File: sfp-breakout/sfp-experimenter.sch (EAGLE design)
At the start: 49 parts, among them IC1 SN65LVDS1DBV, IC2 SN65LVDT2DBV, J1 694108106102, T1 BC847, T2 BC847, U1 LDO-MCP1825S, X1 PINHD-1X5LOCK, X2 PINHD-1X5LOCK, X3 PINHD-1X4LOCK

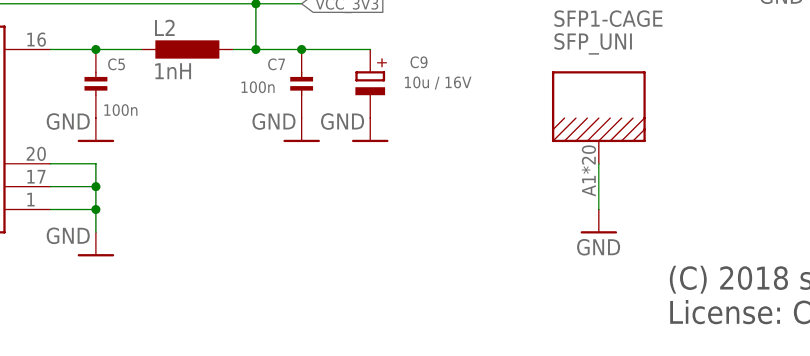
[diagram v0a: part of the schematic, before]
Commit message: sfp: add part numbers for SFP conn and cage
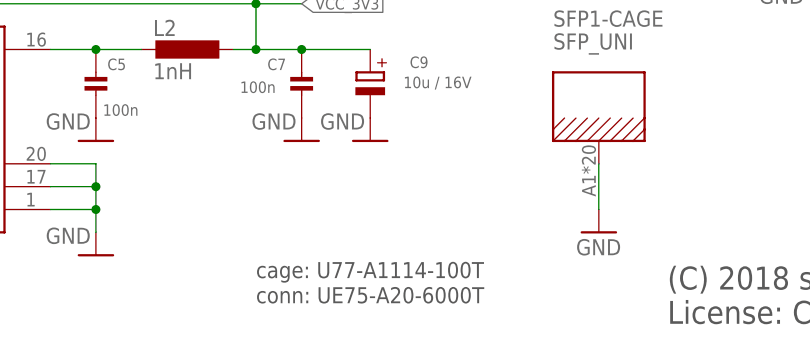
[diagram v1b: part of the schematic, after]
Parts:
- L1, L2: LINK UNKNOWN LINK -> https://www.digikey.de/product-detail/en/samsung-electro-me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
- SFP1: LINK UNKNOWN LINK -> https://www.digikey.de/products/en?keywords=U77-A1114-100TC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
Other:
- note added: "cage: U77-A1114-100T"
- note added: "conn: UE75-A20-6000T"
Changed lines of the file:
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@@
 <attribute name="CLASS" value="UNKNOWN CLASS"/>
 <attribute name="DESCRIPTION" value="NO DESCRIPTION"/>
-<attribute name="LINK" value="UNKNOWN LINK"/>
+<attribute name="LINK" value="https://www.digikey.de/products/en?keywords=U77-A1114-100TCT-ND"/>
 <attribute name="MANUFACTURER" value="UNKNOWN MANUFACTURER"/>
 <attribute name="MANUFACTURERPARTNUMBER" value="UNKNOWN MANUFACTURER PART NUMBER"/>
@@
 <attribute name="CLASS" value="INDUCTOR"/>
 <attribute name="DESCRIPTION" value="NO DESCRIPTION"/>
-<attribute name="LINK" value="UNKNOWN LINK"/>
+<attribute name="LINK" value="https://www.digikey.de/product-detail/en/samsung-electro-mechanics/CIH10T1N0SNC/1276-6301-1-ND"/>
 <attribute name="MANUFACTURER" value="UNKNOWN MANUFACTURER"/>
 <attribute name="MANUFACTURERPARTNUMBER" value="UNKNOWN MANUFACTURER PART NUMBER"/>
@@
 <attribute name="CLASS" value="INDUCTOR"/>
 <attribute name="DESCRIPTION" value="NO DESCRIPTION"/>
-<attribute name="LINK" value="UNKNOWN LINK"/>
+<attribute name="LINK" value="https://www.digikey.de/product-detail/en/samsung-electro-mechanics/CIH10T1N0SNC/1276-6301-1-ND"/>
 <attribute name="MANUFACTURER" value="UNKNOWN MANUFACTURER"/>
 <attribute name="MANUFACTURERPARTNUMBER" value="UNKNOWN MANUFACTURER PART NUMBER"/>
@@
 License: CC-BY-SA</text>
 <text x="119.38" y="96.52" size="3.81" layer="97">3,3 V LDO</text>
+<text x="116.84" y="15.24" size="1.778" layer="97">cage: U77-A1114-100T</text>
+<text x="116.84" y="12.446" size="1.778" layer="97">conn: UE75-A20-6000T</text>
 </plain>
 <instances>

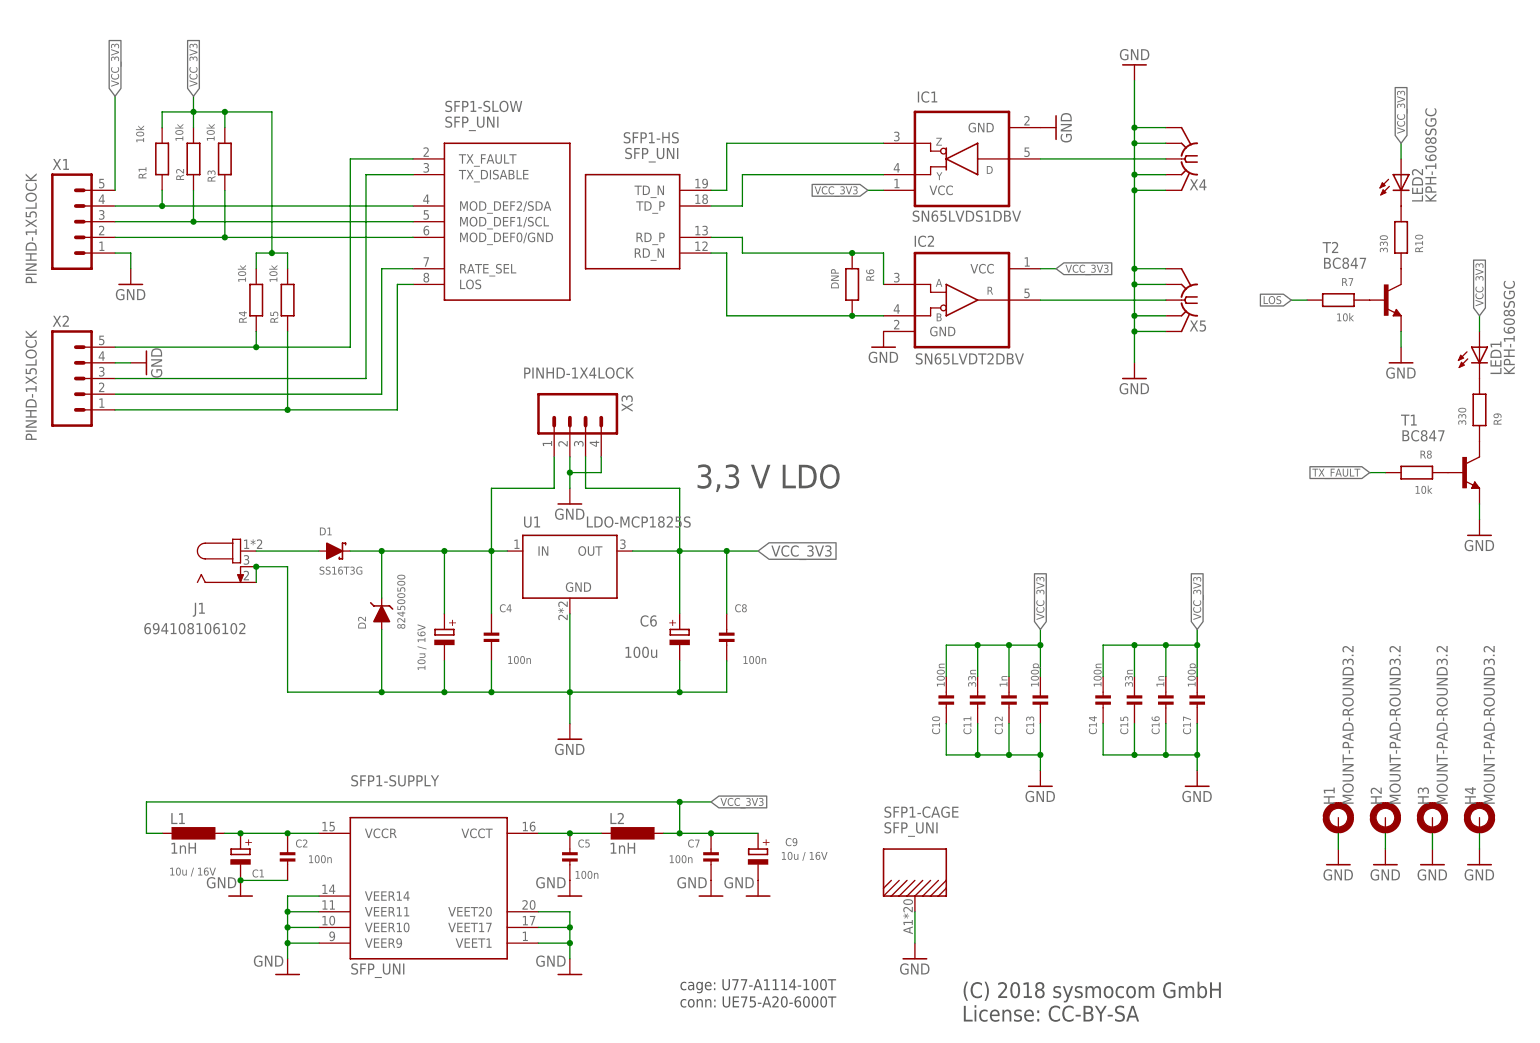
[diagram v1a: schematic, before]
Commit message: sfp-*: add OSHW logo, fill ext'd attribs for BOM
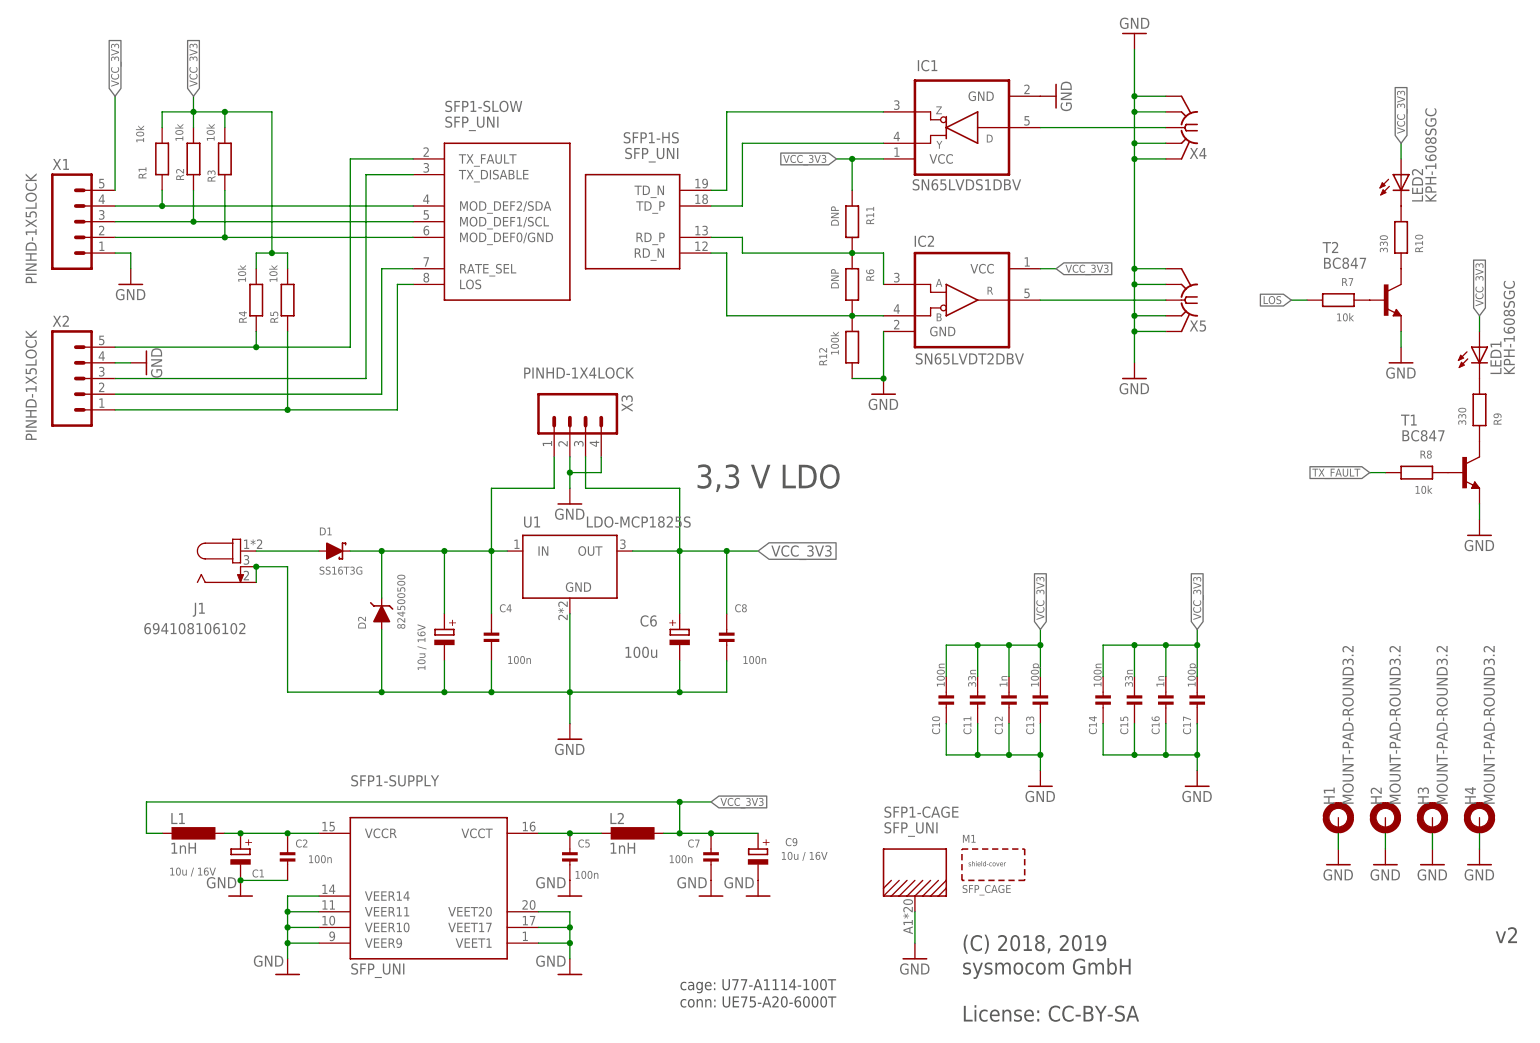
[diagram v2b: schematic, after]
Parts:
- added R11: DNP, sfp-experimenter:RESISTOR_0603
- added R12: 100k, rc-sysmocom:RESISTOR_0603
- C1, C10, C14, C2, C3, C4, C5, C7, C8, C9, J1, R1, R2, R3, R4, R5: ROHSCERTIFICATE UNKNOWN ROHS CERTIFICATE -> Bleifrei / RoHS-konform
- C11, C15: DESCRIPTION NO DESCRIPTION -> CAP CER 0.033UF 50V X7R 0603; LINK UNKNOWN LINK -> https://www.digikey.de/product-detail/de/avx-corporation/06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; MANUFACTURER UNKNOWN MANUFACTURER -> AVX Corporation; MANUFACTURERPARTNUMBER UNKNOWN MANUFACTURER PART NUMBER -> 06035C333JAT2A; ROHSCERTIFICATE UNKNOWN ROHS CERTIFICATE -> Bleifrei / RoHS-konform; SOURCE UNKNOWN SOURCE -> DIGIKEY; SOURCEPARTNUMBER UNKNOWN SOURCE PART NUMBER -> 478-3723-1-ND
- C12, C16: DESCRIPTION NO DESCRIPTION -> CAP CER 1000PF 50V X7R 0603; LINK UNKNOWN LINK -> https://www.digikey.de/product-detail/de/yageo/CC0603KRX7R9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; MANUFACTURER UNKNOWN MANUFACTURER -> Yageo; MANUFACTURERPARTNUMBER UNKNOWN MANUFACTURER PART NUMBER -> CC0603KRX7R9BB102; ROHSCERTIFICATE UNKNOWN ROHS CERTIFICATE -> Bleifrei / RoHS-konform; SOURCE UNKNOWN SOURCE -> DIGIKEY; SOURCEPARTNUMBER UNKNOWN SOURCE PART NUMBER -> 311-1080-1-ND
- C13, C17: DESCRIPTION NO DESCRIPTION -> CAP CER 100PF 50V C0G/NPO 0603; LINK UNKNOWN LINK -> https://www.digikey.de/product-detail/de/yageo/CC0603JRNPO9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; MANUFACTURER UNKNOWN MANUFACTURER -> Yageo; MANUFACTURERPARTNUMBER UNKNOWN MANUFACTURER PART NUMBER -> CC0603JRNPO9BN101; ROHSCERTIFICATE UNKNOWN ROHS CERTIFICATE -> Bleifrei / RoHS-konform; SOURCE UNKNOWN SOURCE -> DIGIKEY; SOURCEPARTNUMBER UNKNOWN SOURCE PART NUMBER -> 311-1069-1-ND
- C6: DESCRIPTION CAP TANT 100UF 6.3V 10% 2413 -> CAP TANT 100UF 10%% 6.3V 2312; LINK http://www.digikey.de/product-detail/de/T491C107K006AT/399-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 -> https://www.digikey.de/product-detail/de/avx-corporation/TP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; MANUFACTURER Kemet -> AVX Corporation; MANUFACTURERPARTNUMBER T491C107K006AT -> TPSC107K006R0150; SOURCEPARTNUMBER 399-8337-1-ND -> 478-1764-1-ND
- D2: DESCRIPTION NO DESCRIPTION -> TVS DIODE 5V 9.2V DO214AC; MANUFACTURER UNKNOWN MANUFACTURER -> Wurth Electronics Inc.; MANUFACTURERPARTNUMBER UNKNOWN MANUFACTURER PART NUMBER -> 824500500; ROHSCERTIFICATE UNKNOWN ROHS CERTIFICATE -> Bleifrei / RoHS-konform; SOURCE UNKNOWN SOURCE -> DIGIKEY; SOURCEPARTNUMBER UNKNOWN SOURCE PART NUMBER -> 732-9974-1-ND
- IC1: CLASS UNKNOWN CLASS -> IC; DESCRIPTION NO DESCRIPTION -> IC 1/0 DRIVER LVDS SOT23-5; LINK UNKNOWN LINK -> https://www.digikey.de/product-detail/de/texas-instruments/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; MANUFACTURER UNKNOWN MANUFACTURER -> Texas Instruments; MANUFACTURERPARTNUMBER UNKNOWN MANUFACTURER PART NUMBER -> SN65LVDS1DBVR; ROHSCERTIFICATE UNKNOWN ROHS CERTIFICATE -> Bleifrei / RoHS-konform; SOURCE UNKNOWN SOURCE -> DIGIKEY; SOURCEPARTNUMBER UNKNOWN SOURCE PART NUMBER -> 296-6919-1-ND
- IC2: CLASS UNKNOWN CLASS -> IC; DESCRIPTION NO DESCRIPTION -> IC DIFF LINE RECEIVER SOT-23-5; LINK UNKNOWN LINK -> https://www.digikey.de/product-detail/de/texas-instruments/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; MANUFACTURER UNKNOWN MANUFACTURER -> Texas Instruments; MANUFACTURERPARTNUMBER UNKNOWN MANUFACTURER PART NUMBER -> SN65LVDT2DBVR; ROHSCERTIFICATE UNKNOWN ROHS CERTIFICATE -> Bleifrei / RoHS-konform; SOURCE UNKNOWN SOURCE -> DIGIKEY; SOURCEPARTNUMBER UNKNOWN SOURCE PART NUMBER -> 296-6896-1-ND
- L1, L2: DESCRIPTION NO DESCRIPTION -> FIXED IND 1NH 800MA 50 MOHM SMD; LINK https://www.digikey.de/product-detail/en/samsung-electro-me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 -> https://www.digikey.de/product-detail/de/samsung-electro-me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; MANUFACTURER UNKNOWN MANUFACTURER -> Samsung Electro-Mechanics; MANUFACTURERPARTNUMBER UNKNOWN MANUFACTURER PART NUMBER -> CIH10T1N0SNC; ROHSCERTIFICATE UNKNOWN ROHS CERTIFICATE -> Bleifrei / RoHS-konform; SOURCE UNKNOWN SOURCE -> DIGIKEY; SOURCEPARTNUMBER UNKNOWN SOURCE PART NUMBER -> 1276-6301-1-ND
- R6: POPULATED TRUE -> FALSE
- SFP1: CLASS UNKNOWN CLASS -> SFP; DESCRIPTION NO DESCRIPTION -> CONN SFP RCPT 20POS SLD R/A SMD; LINK https://www.digikey.de/products/en?keywords=U77-A1114-100TC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 -> https://www.digikey.de/product-detail/de/amphenol-icc-comme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; MANUFACTURER UNKNOWN MANUFACTURER -> Amphenol ICC (Commercial Products); MANUFACTURERPARTNUMBER UNKNOWN MANUFACTURER PART NUMBER -> UE75-A20-6000T; ROHSCERTIFICATE UNKNOWN ROHS CERTIFICATE -> Bleifrei / RoHS-konform; SOURCE UNKNOWN SOURCE -> DIGIKEY; SOURCEPARTNUMBER UNKNOWN SOURCE PART NUMBER -> UE75-A20-6000TCT-ND
- U1: DESCRIPTION NO DESCRIPTION -> IC REG LIN 3.3V 500MA SOT223-3; MANUFACTURER UNKNOWN MANUFACTURER -> Microchip Technology; MANUFACTURERPARTNUMBER UNKNOWN MANUFACTURER PART NUMBER -> MCP1825ST-3302E/DB; ROHSCERTIFICATE UNKNOWN ROHS CERTIFICATE -> Bleifrei / RoHS-konform; SOURCE UNKNOWN SOURCE -> DIGIKEY; SOURCEPARTNUMBER UNKNOWN SOURCE PART NUMBER -> MCP1825ST-3302E/DBCT-ND
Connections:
- net GND: now also R12.2
- net RD_N: now also R12.1
- net RD_P: now also R11.2
- net VCC_3V3: now also R11.1
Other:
- note added: "(C) 2018, 2019 sysmocom GmbH License: CC-BY-SA"
- note removed: "(C) 2018 sysmocom GmbH License: CC-BY-SA"
- moved on the sheet: IC1, X4

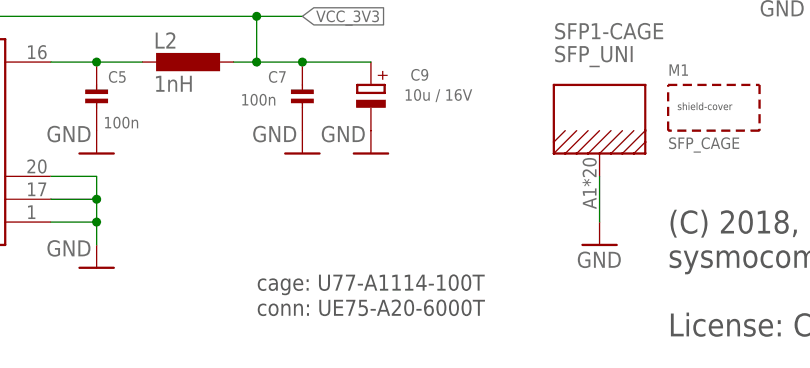
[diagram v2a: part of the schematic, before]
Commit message: sfp-experimenter: update SFP cage part number
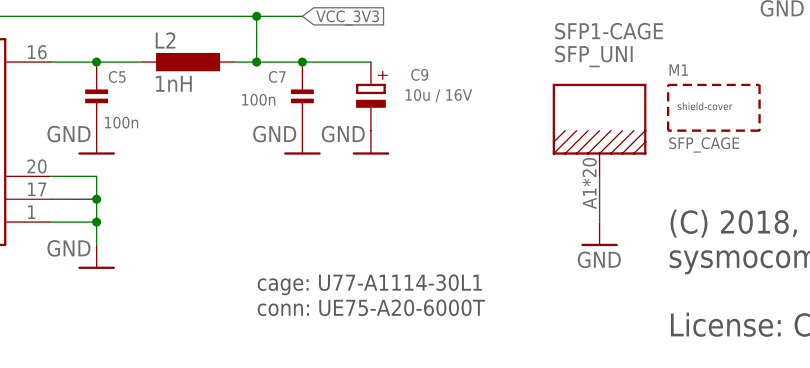
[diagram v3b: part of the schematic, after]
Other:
- note added: "cage: U77-A1114-30L1"
- note removed: "cage: U77-A1114-100T"
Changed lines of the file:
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@@
 </part>
 <part name="M1" library="BOM-exclusive" deviceset="SHIELD-COVER" device="" value="SFP_CAGE">
-<attribute name="CLASS" value="SHIELD COVER"/>
 <attribute name="DESCRIPTION" value="CONN SFP CAGE SLD R/A"/>
-<attribute name="LINK" value="https://www.digikey.de/product-detail/de/amphenol-icc-commercial-products/U77-A1114-100T/U77-A1114-100TCT-ND"/>
+<attribute name="LINK" value="https://www.digikey.de/product-detail/de/amphenol-icc-commercial-products/U77-A1114-30L1/U77-A1114-30L1-ND"/>
 <attribute name="MANUFACTURER" value="Amphenol ICC (Commercial Products)"/>
-<attribute name="MANUFACTURERPARTNUMBER" value="U77-A1114-100T"/>
-<attribute name="ROHSCERTIFICATE" value="Bleifrei / RoHS-konform"/>
+<attribute name="MANUFACTURERPARTNUMBER" value="U77-A1114-30L1"/>
 <attribute name="SOURCE" value="DIGIKEY"/>
-<attribute name="SOURCEPARTNUMBER" value="U77-A1114-100TCT-ND"/>
+<attribute name="SOURCEPARTNUMBER" value="U77-A1114-30L1-ND"/>
 </part>
 </parts>
@@
 License: CC-BY-SA</text>
 <text x="119.38" y="96.52" size="3.81" layer="97">3,3 V LDO</text>
-<text x="116.84" y="15.24" size="1.778" layer="97">cage: U77-A1114-100T</text>
+<text x="116.84" y="15.24" size="1.778" layer="97">cage: U77-A1114-30L1</text>
 <text x="116.84" y="12.446" size="1.778" layer="97">conn: UE75-A20-6000T</text>
 <text x="248.92" y="22.86" size="2.54" layer="97">&gt;VERSION</text>

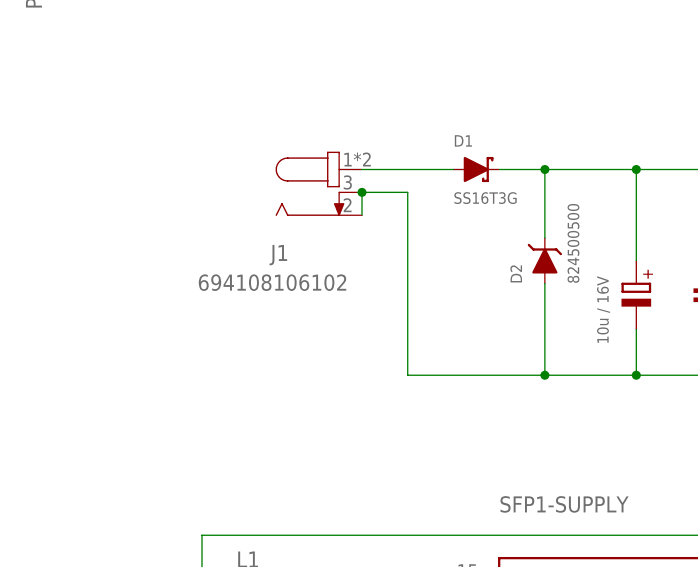
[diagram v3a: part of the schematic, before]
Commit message: sfp-experimenter: update ext'd attribs and BOM
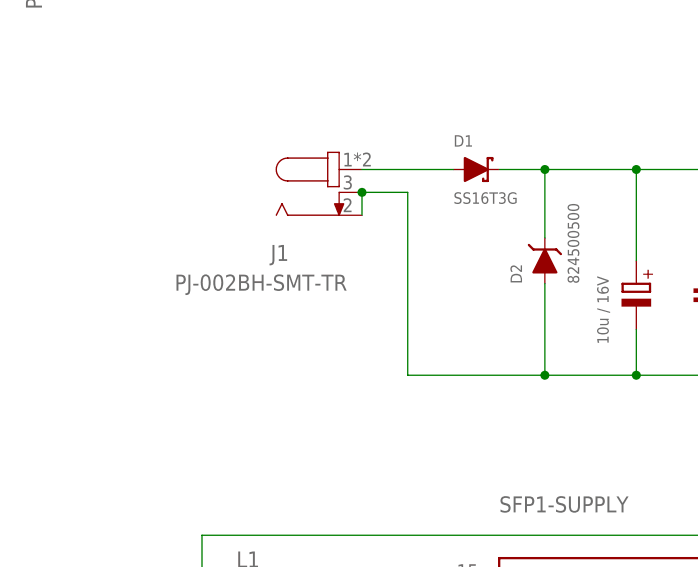
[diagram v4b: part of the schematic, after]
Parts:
- C6: DESCRIPTION CAP TANT 100UF 10%% 6.3V 2312 -> CAP TANT POLY 100UF 6.3V 2312; LINK https://www.digikey.de/product-detail/de/avx-corporation/TP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 -> https://www.digikey.de/product-detail/de/kemet/T520C107M006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; MANUFACTURER AVX Corporation -> KEMET; MANUFACTURERPARTNUMBER TPSC107K006R0150 -> T520C107M006ATE045; ROHSCERTIFICATE Bleifrei / RoHS-konform -> UNKNOWN ROHS CERTIFICATE; SOURCEPARTNUMBER 478-1764-1-ND -> 399-4658-1-ND
- J1: value 694108106102 -> PJ-002BH-SMT-TR; LINK https://www.digikey.de/product-detail/de/wurth-electronics-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 -> https://www.digikey.de/product-detail/de/cui-inc/PJ-002BH-S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; MANUFACTURER Wurth Electronics Inc. -> CUI Devices; MANUFACTURERPARTNUMBER 694108106102 -> PJ-002BH-SMT-TR; ROHSCERTIFICATE Bleifrei / RoHS-konform -> UNKNOWN ROHS CERTIFICATE; SOURCEPARTNUMBER 732-5933-1-ND -> CP-002BHPJCT-ND
- L1, L2: DESCRIPTION FIXED IND 1NH 800MA 50 MOHM SMD -> FIXED IND 1NH 500MA 50 MOHM SMD; LINK https://www.digikey.de/product-detail/de/samsung-electro-me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 -> https://www.digikey.de/product-detail/de/abracon-llc/AIMC-0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; MANUFACTURER Samsung Electro-Mechanics -> Abracon LLC; MANUFACTURERPARTNUMBER CIH10T1N0SNC -> AIMC-0603-1N0S-T; ROHSCERTIFICATE Bleifrei / RoHS-konform -> UNKNOWN ROHS CERTIFICATE; SOURCEPARTNUMBER 1276-6301-1-ND -> 535-11529-1-ND
- R1, R2, R3, R4, R5: DESCRIPTION RES 10K OHM 1%% 1/10W 0603 -> RES SMD 10K OHM 1%% 1/10W 0603; LINK https://www.digikey.de/product-detail/de/stackpole-electron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 -> https://www.digikey.de/product-detail/de/yageo/RC0603FR-071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; MANUFACTURER Stackpole Electronics Inc. -> Yageo; MANUFACTURERPARTNUMBER RMCF0603FT10K0 -> RC0603FR-0710KL; ROHSCERTIFICATE Bleifrei / RoHS-konform -> UNKNOWN ROHS CERTIFICATE; SOURCEPARTNUMBER RMCF0603FT10K0CT-ND -> 311-10.0KHRCT-ND
- R10, R9: DESCRIPTION RES 330 OHM 1/10W 1% 0603 SMD -> RES SMD 330 OHM 5%% 1/10W 0603; LINK http://www.digikey.de/product-detail/de/foo/RHM330CFCT-ND -> https://www.digikey.de/product-detail/de/panasonic-electron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; MANUFACTURER Rohm Semiconductor -> Panasonic Electronic Components; MANUFACTURERPARTNUMBER MCR03ERTF3300 -> ERJ-3GEYJ331V; ROHSCERTIFICATE Bleifrei / RoHS-konform -> UNKNOWN ROHS CERTIFICATE; SOURCEPARTNUMBER RHM330CFCT-ND -> P330GCT-ND
- R12: DESCRIPTION RES 100K OHM 1/10W 1% 0603 SMD -> RES 100K OHM 1%% 1/10W 0603; LINK http://www.digikey.de/product-detail/de/foo/RHM100KCFCT-ND -> https://www.digikey.de/product-detail/de/koa-speer-electron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; MANUFACTURER Rohm Semiconductor -> KOA Speer Electronics, Inc.; MANUFACTURERPARTNUMBER MCR03ERTF1003 -> RK73H1JTTD1003F; ROHSCERTIFICATE Bleifrei / RoHS-konform -> UNKNOWN ROHS CERTIFICATE; SOURCEPARTNUMBER RHM100KCFCT-ND -> 2019-RK73H1JTTD1003FCT-ND
- R7, R8: DESCRIPTION RES 10K OHM 1/10W 1% 0603 SMD -> RES SMD 10K OHM 1%% 1/10W 0603; LINK http://www.digikey.de/product-detail/de/foo/RHM10.0KCFCT-ND -> https://www.digikey.de/product-detail/de/yageo/RC0603FR-071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; MANUFACTURER Rohm Semiconductor -> Yageo; MANUFACTURERPARTNUMBER MCR03ERTF1002 -> RC0603FR-0710KL; ROHSCERTIFICATE Bleifrei / RoHS-konform -> UNKNOWN ROHS CERTIFICATE; SOURCEPARTNUMBER RHM10.0KCFCT-ND -> 311-10.0KHRCT-ND
